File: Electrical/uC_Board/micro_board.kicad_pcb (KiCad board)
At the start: 2 copper layers, 43.6 x 18 mm, 22 parts, among them J1 card_edge_6p, U1 ATmega328PB-AU, U2 ArdStripNano, U3 CSTNE16M0V530000R0, U4 AD8620-hodgkin, U5 LM1117MPX-5.0

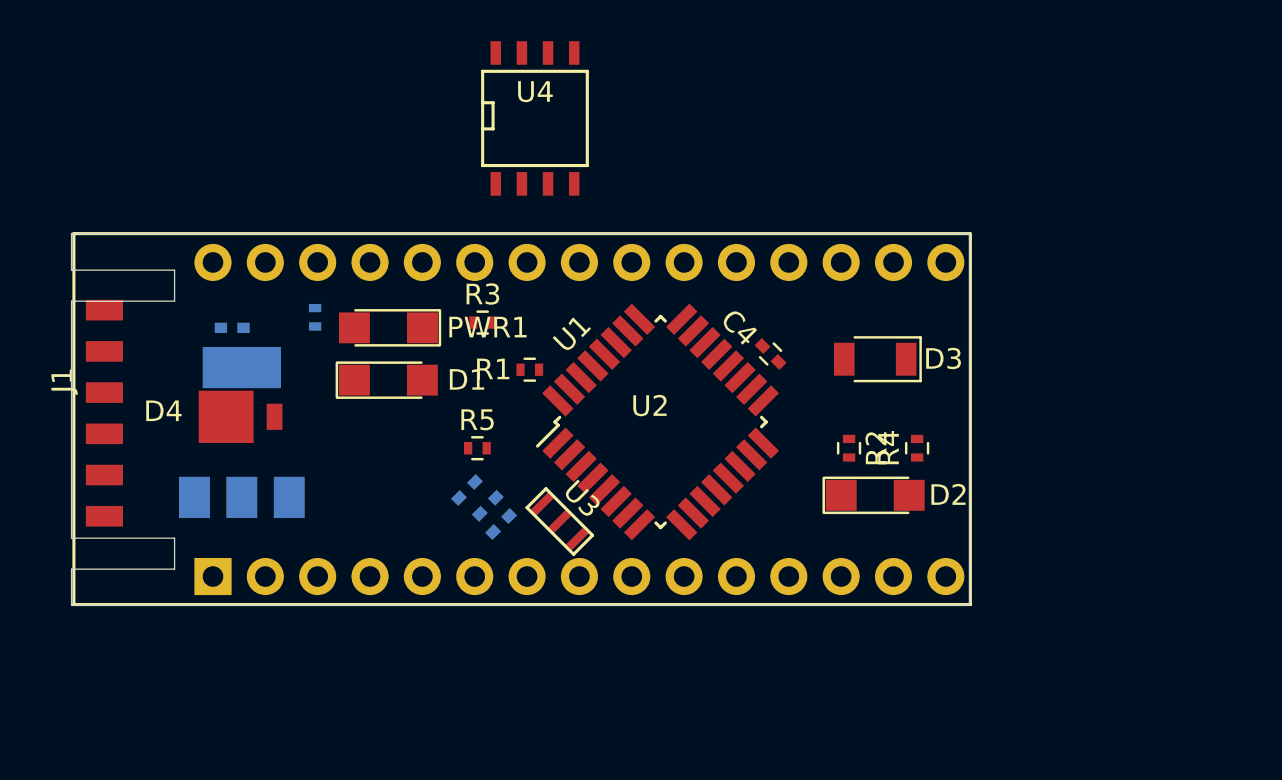
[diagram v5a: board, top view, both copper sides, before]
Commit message: changed sizes of resistors and capacitors, trying to neatly lay things out on pcb
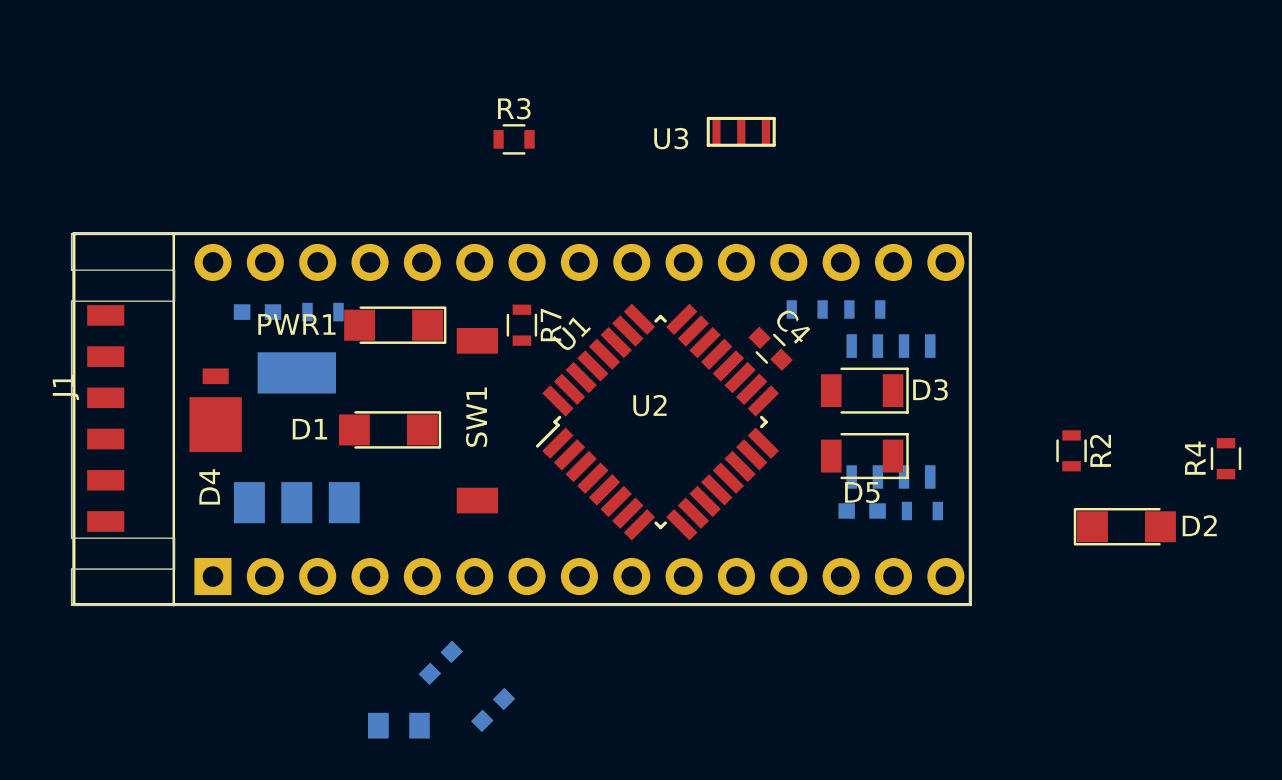
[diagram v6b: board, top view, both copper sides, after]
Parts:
- added C6: 100nF, Capacitors_SMD:C_0603, B.Cu at (137.0, 115.1)
- added D5: D_Photo, Diodes_SMD:D_1206, F.Cu at (137.0, 112.4)
- added R7: 1k, Resistors_SMD:R_0603, F.Cu at (120.5, 106.0)
- added R8: 1M, Resistors_SMD:R_0603, B.Cu at (140.0, 115.1)
- added SW1: SW_Push, hodgkin:PTS636-G-2.5-NoGND, F.Cu at (118.4, 114.6)
- C1, C3, C4, C5: footprint Capacitors_SMD:C_0402 -> Capacitors_SMD:C_0603
- C2: footprint Capacitors_SMD:C_0402 -> Capacitors_SMD:C_0805
- R1, R5: footprint Resistors_SMD:R_0402 -> Resistors_SMD:R_0603; moved to B.Cu
- R2, R3, R4, R6: footprint Resistors_SMD:R_0402 -> Resistors_SMD:R_0603
- U4: value AD8620-hodgkin -> AD8620; moved to B.Cu
- U5: footprint TO_SOT_Packages_SMD:SOT-223 -> hodgkin:LM1117
- moved U4 22.4 mm to (138.4, 110.2)
- moved R5 20.0 mm to (137.2, 105.3)
- moved U3 19.7 mm to (129.6, 97.3), turned to 0 degrees
- moved R4 15.0 mm to (154.7, 112.5)
- moved R1 13.8 mm to (134.4, 105.3), turned to 180 degrees
- moved D2 12.3 mm to (149.9, 115.8)
- moved C2 11.5 mm to (114.6, 125.5), turned to 0 degrees
- moved R2 10.8 mm to (147.2, 112.1)
- moved C1 9.03 mm to (119.1, 124.7)
- moved R3 9.02 mm to (120.1, 97.0)
- moved C3 8.48 mm to (116.6, 122.4)
- moved U5 2.68 mm to (109.6, 111.5)
- moved D1 2.41 mm to (114.0, 111.1), turned to 180 degrees
- moved D3 1.65 mm to (137.0, 109.2)
- moved C5 1.45 mm to (107.7, 105.4)
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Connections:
- R5 pad 1: Net-(D3-Pad1) -> /RX
- R5 pad 2: /RX -> Net-(D3-Pad1)
- U4 pad 3: (no net) -> GND
- U4 pad 4: (no net) -> GND
- U4 pad 5: Net-(U4-Pad5) -> GND
- U5 pad 1: Net-(U5-Pad1) -> GND

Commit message: trying to do stuff idk
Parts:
- moved PWR1 0.38 mm to (113.9, 106.0)
- moved SW1 0.25 mm to (118.6, 114.6)
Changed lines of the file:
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@@
   (general
     (thickness 1.6)
-    (drawings 13)
+    (drawings 14)
     (tracks 0)
     (zones 0)
@@
   )
   (module hodgkin:PTS636-G-2.5-NoGND (layer F.Cu)
-    (at 118.364 114.554 90)
+    (at 118.618 114.554 90)
     (fp_text reference SW1 (at 4.064 0 90) (layer F.SilkS)
       (effects (font (size 1 1) (thickness 0.15)))
@@
   )
   (module LEDs:LED_1206 (layer F.Cu)
-    (at 114.3 106.045 180)
+    (at 113.919 106.045 180)
     (descr "LED 1206 smd package")
     (tags "LED led 1206 SMD smd SMT smt smdled SMDLED smtled SMTLED")
@@
     )
   )
+  (gr_line (start 94.996 111.63) (end 152.146 111.63) (layer Dwgs.User) (width 0.15))
   (gr_line (start 103.632 101.6) (end 103.632 119.634) (layer F.SilkS) (width 0.12))
   (gr_line (start 142.244 101.596) (end 98.67 101.596) (layer Edge.Cuts) (width 0.05))

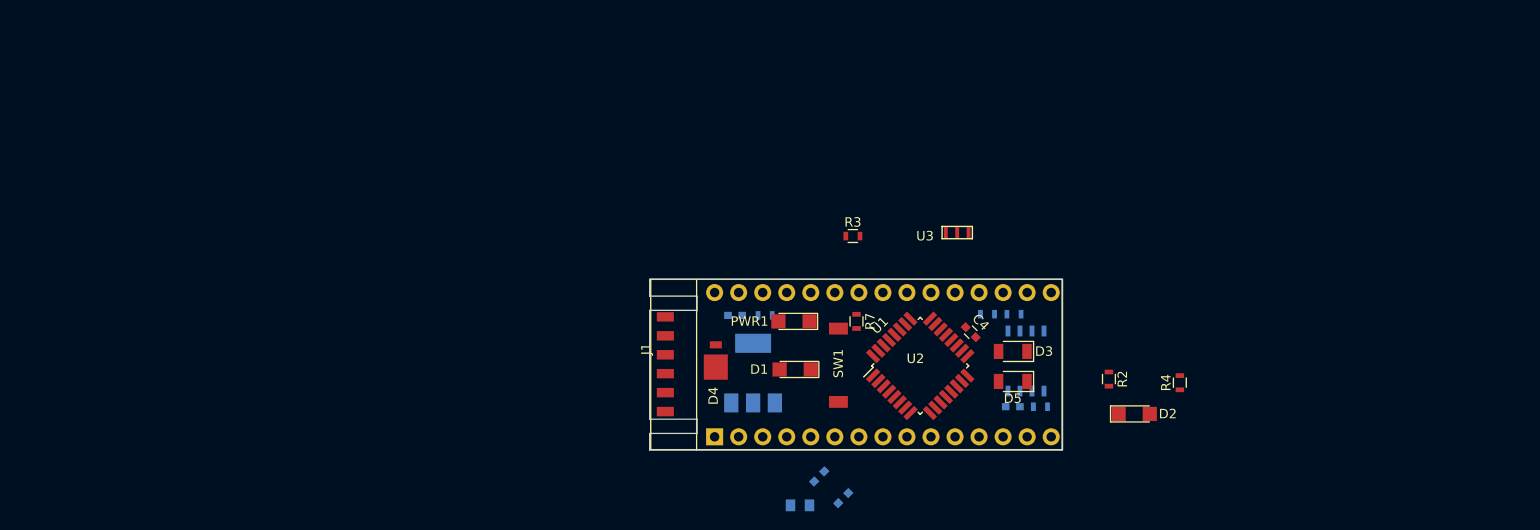
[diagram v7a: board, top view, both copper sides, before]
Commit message: locking in LED and PDs
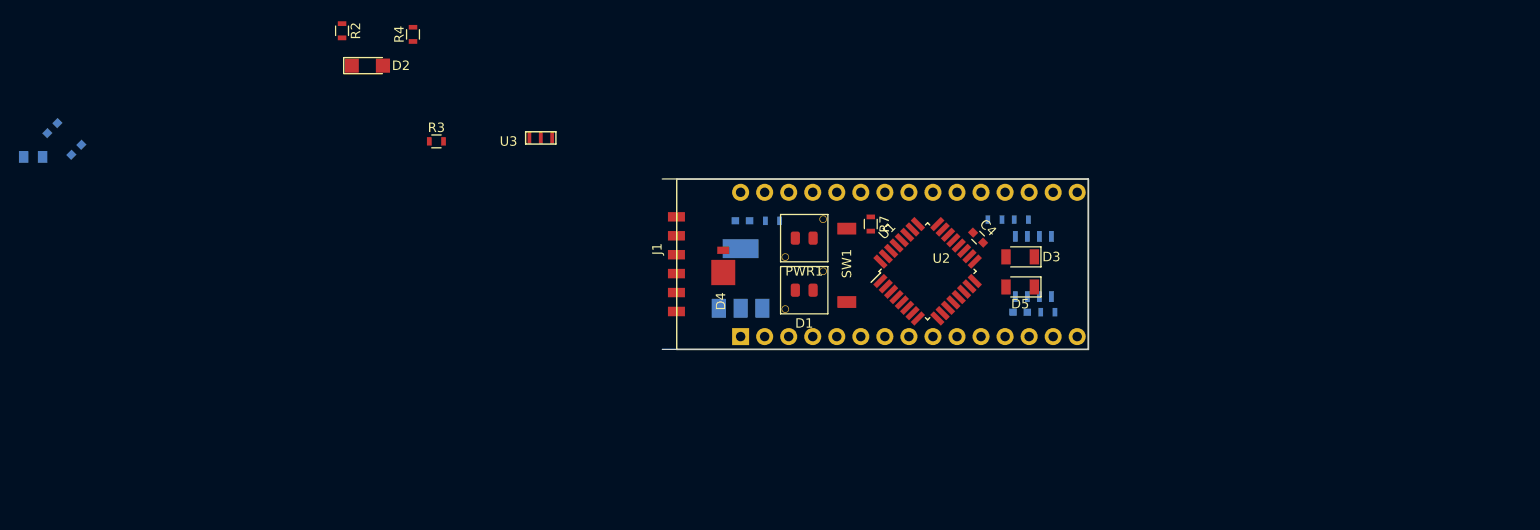
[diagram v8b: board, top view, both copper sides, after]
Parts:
- D1, PWR1: footprint LEDs:LED_1206 -> hodgkin:LED_0805_LightPipe
- moved R2 89.0 mm to (66.2, 75.3)
- moved R4 89.0 mm to (73.7, 75.7)
- moved C1 89.0 mm to (38.1, 87.9)
- moved C2 89.0 mm to (33.5, 88.7)
- moved D2 89.0 mm to (68.8, 79.0)
- moved C3 89.0 mm to (35.6, 85.6)
- moved R3 45.1 mm to (76.1, 87.0)
- moved U3 45.1 mm to (85.6, 87.3)
- moved U2 10.9 mm to (147.8, 91.0)
- moved J1 10.6 mm to (101.5, 105.0)
- moved SW1 10.6 mm to (119.5, 104.0)
- moved R7 10.4 mm to (122.0, 95.8)
- moved U5 10.1 mm to (108.3, 101.5)
- moved C4 10.0 mm to (133.4, 97.2)
- moved U4 10.0 mm to (139.2, 100.2)
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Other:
- board size 43.6 x 18 mm -> 45 x 18 mm
